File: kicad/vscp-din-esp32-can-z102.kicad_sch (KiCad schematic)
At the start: 33 parts, among them J1 Conn_01x05, J2 Conn_01x02, J3 Conn_01x06, J4 Conn_01x04, J5 Conn_01x04, J6 Conn_01x03, U1 ESP32-C3-WROOM-02-N4, U2 LM2575-3.3BT, U3 SN65HVD232, U4 R-78B3.3-1.0 (Recom)

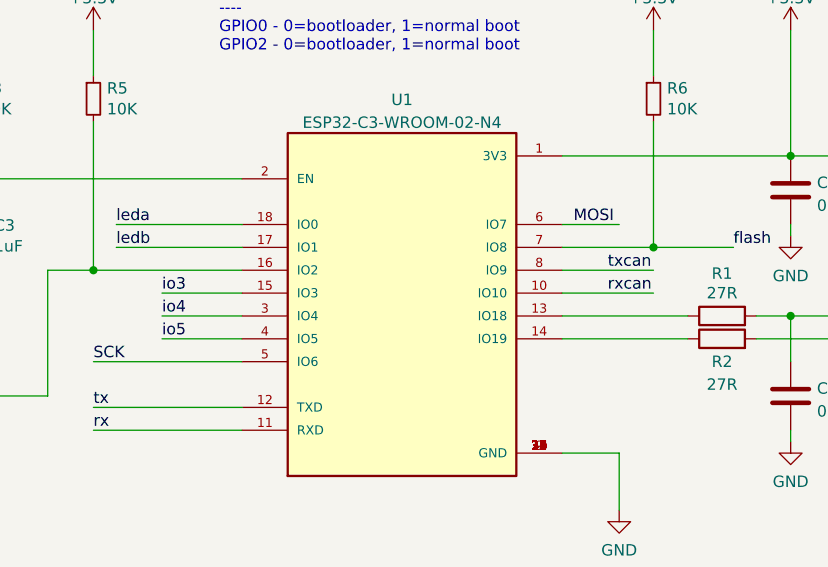
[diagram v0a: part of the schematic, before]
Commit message: rev b schame started canrx moved from gpio10 to gpio3
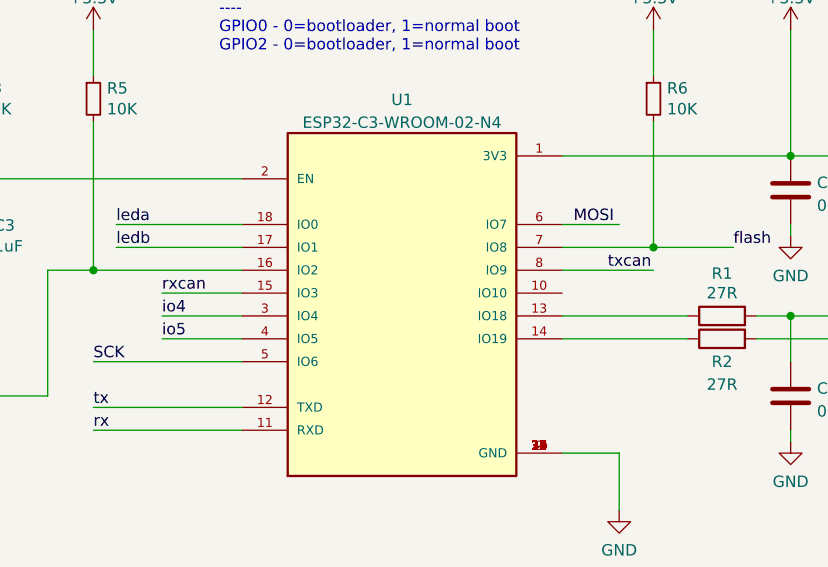
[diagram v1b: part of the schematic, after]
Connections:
- net io3 is gone; now on net rxcan: U1.15 (IO3)
- net rxcan: no longer U1.10 (IO10)
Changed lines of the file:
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@@
-    (stroke (width 0) (type default) (color 0 0 0 0))
-  )
-  (wire (pts (xy 134.62 57.15) (xy 144.78 57.15))
     (stroke (width 0) (type default) (color 0 0 0 0))
   )
@@
     (stroke (width 0) (type default) (color 0 0 0 0))
   )
+  (wire (pts (xy 68.58 46.99) (xy 68.58 44.45))
+    (stroke (width 0) (type default) (color 0 0 0 0))
+  )
+  (wire (pts (xy 262.89 148.59) (xy 262.89 153.67))
+    (stroke (width 0) (type default) (color 0 0 0 0))
+  )
+  (wire (pts (xy 82.55 107.95) (xy 97.79 107.95))
+    (stroke (width 0) (type default) (color 0 0 0 0))
+  )
+  (wire (pts (xy 148.59 121.92) (xy 160.02 121.92))
+    (stroke (width 0) (type default) (color 0 0 0 0))
+  )
+  (wire (pts (xy 208.28 81.28) (xy 215.9 81.28))
+    (stroke (width 0) (type default) (color 0 0 0 0))
+  )
+  (wire (pts (xy 240.03 93.98) (xy 240.03 97.79))
+    (stroke (width 0) (type default) (color 0 0 0 0))
+  )
+  (wire (pts (xy 138.43 158.75) (xy 138.43 160.02))
+    (stroke (width 0) (type default) (color 0 0 0 0))
+  )
+  (wire (pts (xy 144.78 52.07) (xy 153.67 52.07))
+    (stroke (width 0) (type default) (color 0 0 0 0))
+  )
+  (wire (pts (xy 160.02 129.54) (xy 160.02 156.21))
+    (stroke (width 0) (type default) (color 0 0 0 0))
+  )
+  (wire (pts (xy 90.17 62.23) (xy 99.06 62.23))
+    (stroke (width 0) (type default) (color 0 0 0 0))
+  )
+  (wire (pts (xy 99.06 54.61) (xy 82.55 54.61))
+    (stroke (width 0) (type default) (color 0 0 0 0))
+  )
+  (wire (pts (xy 134.62 52.07) (xy 144.78 52.07))
+    (stroke (width 0) (type default) (color 0 0 0 0))
+  )
+  (wire (pts (xy 226.06 35.56) (xy 226.06 26.67))
+    (stroke (width 0) (type default) (color 0 0 0 0))
+  )
   (wire (pts (xy 90.17 57.15) (xy 99.06 57.15))
-    (stroke (width 0) (type default) (color 0 0 0 0))
-  )
-  (wire (pts (xy 68.58 46.99) (xy 68.58 44.45))
-    (stroke (width 0) (type default) (color 0 0 0 0))
-  )
-  (wire (pts (xy 262.89 148.59) (xy 262.89 153.67))
-    (stroke (width 0) (type default) (color 0 0 0 0))
-  )
-  (wire (pts (xy 82.55 107.95) (xy 97.79 107.95))
-    (stroke (width 0) (type default) (color 0 0 0 0))
-  )
-  (wire (pts (xy 148.59 121.92) (xy 160.02 121.92))
-    (stroke (width 0) (type default) (color 0 0 0 0))
-  )
-  (wire (pts (xy 208.28 81.28) (xy 215.9 81.28))
-    (stroke (width 0) (type default) (color 0 0 0 0))
-  )
-  (wire (pts (xy 240.03 93.98) (xy 240.03 97.79))
-    (stroke (width 0) (type default) (color 0 0 0 0))
-  )
-  (wire (pts (xy 138.43 158.75) (xy 138.43 160.02))
-    (stroke (width 0) (type default) (color 0 0 0 0))
-  )
-  (wire (pts (xy 144.78 52.07) (xy 153.67 52.07))
-    (stroke (width 0) (type default) (color 0 0 0 0))
-  )
-  (wire (pts (xy 160.02 129.54) (xy 160.02 156.21))
-    (stroke (width 0) (type default) (color 0 0 0 0))
-  )
-  (wire (pts (xy 90.17 62.23) (xy 99.06 62.23))
-    (stroke (width 0) (type default) (color 0 0 0 0))
-  )
-  (wire (pts (xy 99.06 54.61) (xy 82.55 54.61))
-    (stroke (width 0) (type default) (color 0 0 0 0))
-  )
-  (wire (pts (xy 134.62 52.07) (xy 144.78 52.07))
-    (stroke (width 0) (type default) (color 0 0 0 0))
-  )
-  (wire (pts (xy 226.06 35.56) (xy 226.06 26.67))
     (stroke (width 0) (type default) (color 0 0 0 0))
   )
@@
     (effects (font (size 1.27 1.27)) (justify left bottom))
   )
-  (label "rxcan" (at 139.7 57.15 0)
+  (label "rxcan" (at 90.17 57.15 0)
     (effects (font (size 1.27 1.27)) (justify left bottom))
   )
@@
     (effects (font (size 1.27 1.27)) (justify left bottom))
   )
-  (label "io3" (at 90.17 57.15 0)
-    (effects (font (size 1.27 1.27)) (justify left bottom))
-  )

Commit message: Added images for rev B
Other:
- note removed: "A"
- company: (none) -> Grodans Paradis AB
- title: (none) -> vscp-din-esp32-can-z102
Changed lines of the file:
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@@
 (kicad_sch (version 20211123) (generator eeschema)
   (paper "A4")
+  (title_block
+    (title "vscp-din-esp32-can-z102")
+    (rev "B")
+    (company "Grodans Paradis AB")
+  )
   (junction (at 30.48 156.21) (diameter 0) (color 0 0 0 0)
   )
@@
     (stroke (width 0) (type default) (color 0 0 0 0))
   )
+  (wire (pts (xy 144.78 52.07) (xy 151.13 52.07))
+    (stroke (width 0) (type default) (color 0 0 0 0))
+  )
   (wire (pts (xy 160.02 121.92) (xy 189.23 121.92))
     (stroke (width 0) (type default) (color 0 0 0 0))
@@
   )
   (wire (pts (xy 138.43 158.75) (xy 138.43 160.02))
-    (stroke (width 0) (type default) (color 0 0 0 0))
-  )
-  (wire (pts (xy 144.78 52.07) (xy 153.67 52.07))
     (stroke (width 0) (type default) (color 0 0 0 0))
   )
@@
     (effects (font (size 1.27 1.27)) (justify left bottom))
   )
-  (text "A" (at 270.51 194.31 0)
-    (effects (font (size 1.27 1.27)) (justify left bottom))
-  )
   (text "Programming\nInterface" (at 264.16 95.25 0)
     (effects (font (size 1.27 1.27)) (justify left bottom))
@@
     (effects (font (size 1.27 1.27)) (justify left bottom))
   )
-  (label "flash" (at 153.67 52.07 0)
+  (label "flash" (at 146.05 52.07 0)
     (effects (font (size 1.27 1.27)) (justify left bottom))
   )
@@
   )
   (symbol (lib_id "Device:L_Ferrite") (at 87.63 161.29 90) (unit 1)
-    (in_bom yes) (on_board yes) (fields_autoplaced)
-    (property "Reference" "L1" (id 0) (at 87.63 156.1932 90))
+    (in_bom yes) (on_board yes)
+    (property "Reference" "L1" (id 0) (at 87.63 162.56 90))
     (property "Value" "SRR1240-331K" (id 1) (at 87.63 158.7301 90))
     (property "Footprint" "Inductor_SMD:L_Bourns_SRR1260" (id 2) (at 87.63 161.29 0)

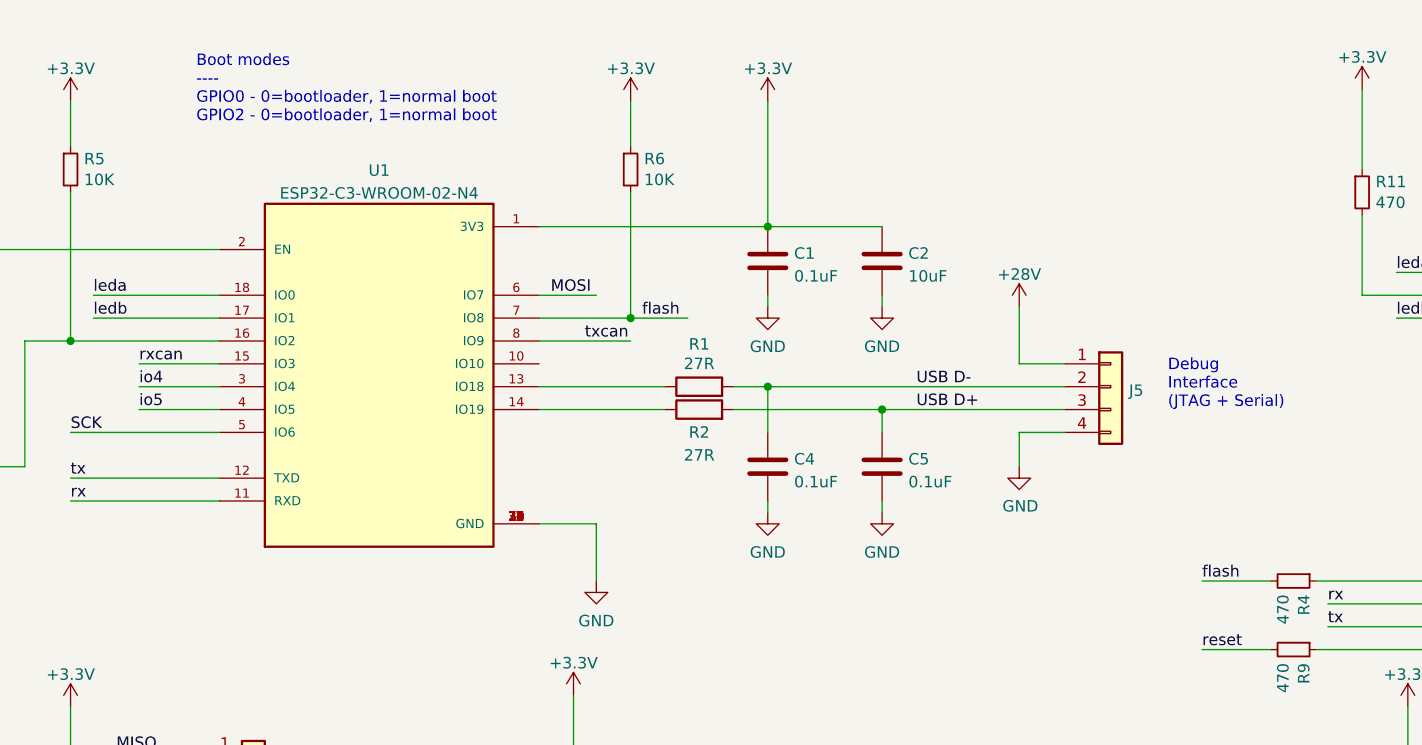
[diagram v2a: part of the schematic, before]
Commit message: txcan routed to Flash pin instead of io8
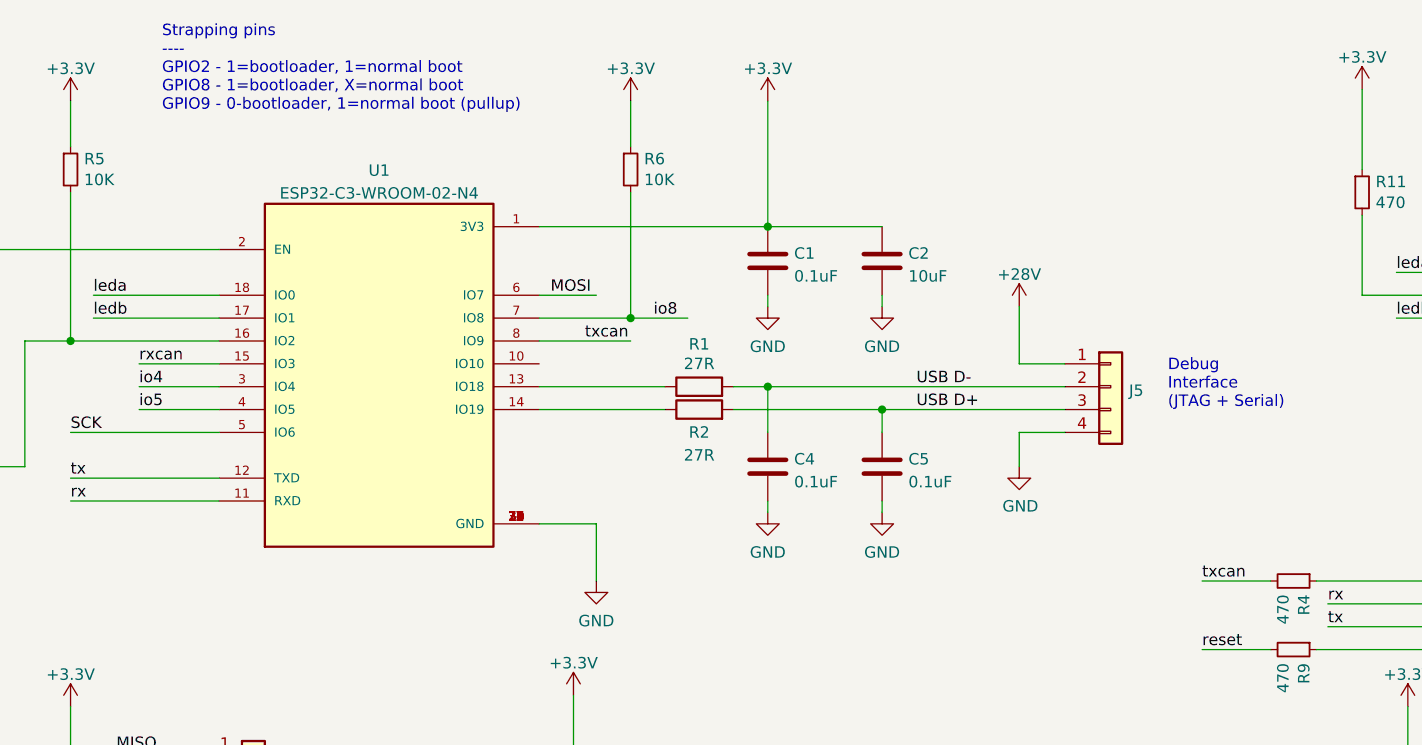
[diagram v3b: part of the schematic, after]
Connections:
- net txcan: now also R4.2
- net flash renamed io8
- net io8: no longer R4.2
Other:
- note added: "Strapping pins ---- GPIO2 - 1=bootloader, 1=normal boot GPIO8 - 1=bootloader, X=normal boot GPIO9 - 0-bootloader, 1=normal boot (pullup)"
- note removed: "Boot modes ---- GPIO0 - 0=bootloader, 1=normal boot GPIO2 - 0=bootloader, 1=normal boot"
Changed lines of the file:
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@@
     (effects (font (size 1.27 1.27)) (justify left bottom))
   )
-  (text "Boot modes\n----\nGPIO0 - 0=bootloader, 1=normal boot\nGPIO2 - 0=bootloader, 1=normal boot"
-    (at 96.52 30.48 0)
+  (text "Strapping pins\n----\nGPIO2 - 1=bootloader, 1=normal boot\nGPIO8 - 1=bootloader, X=normal boot\nGPIO9 - 0-bootloader, 1=normal boot (pullup)"
+    (at 92.71 29.21 0)
     (effects (font (size 1.27 1.27)) (justify left bottom))
   )
@@
     (effects (font (size 1.27 1.27)) (justify left bottom))
   )
-  (label "flash" (at 208.28 81.28 0)
-    (effects (font (size 1.27 1.27)) (justify left bottom))
-  )
   (label "reset" (at 208.28 88.9 0)
     (effects (font (size 1.27 1.27)) (justify left bottom))
@@
   )
   (label "rxcan" (at 90.17 57.15 0)
+    (effects (font (size 1.27 1.27)) (justify left bottom))
+  )
+  (label "io8" (at 147.32 52.07 0)
+    (effects (font (size 1.27 1.27)) (justify left bottom))
+  )
+  (label "txcan" (at 208.28 81.28 0)
     (effects (font (size 1.27 1.27)) (justify left bottom))
   )
@@
     (effects (font (size 1.27 1.27)) (justify left bottom))
   )
-  (label "flash" (at 146.05 52.07 0)
-    (effects (font (size 1.27 1.27)) (justify left bottom))
-  )

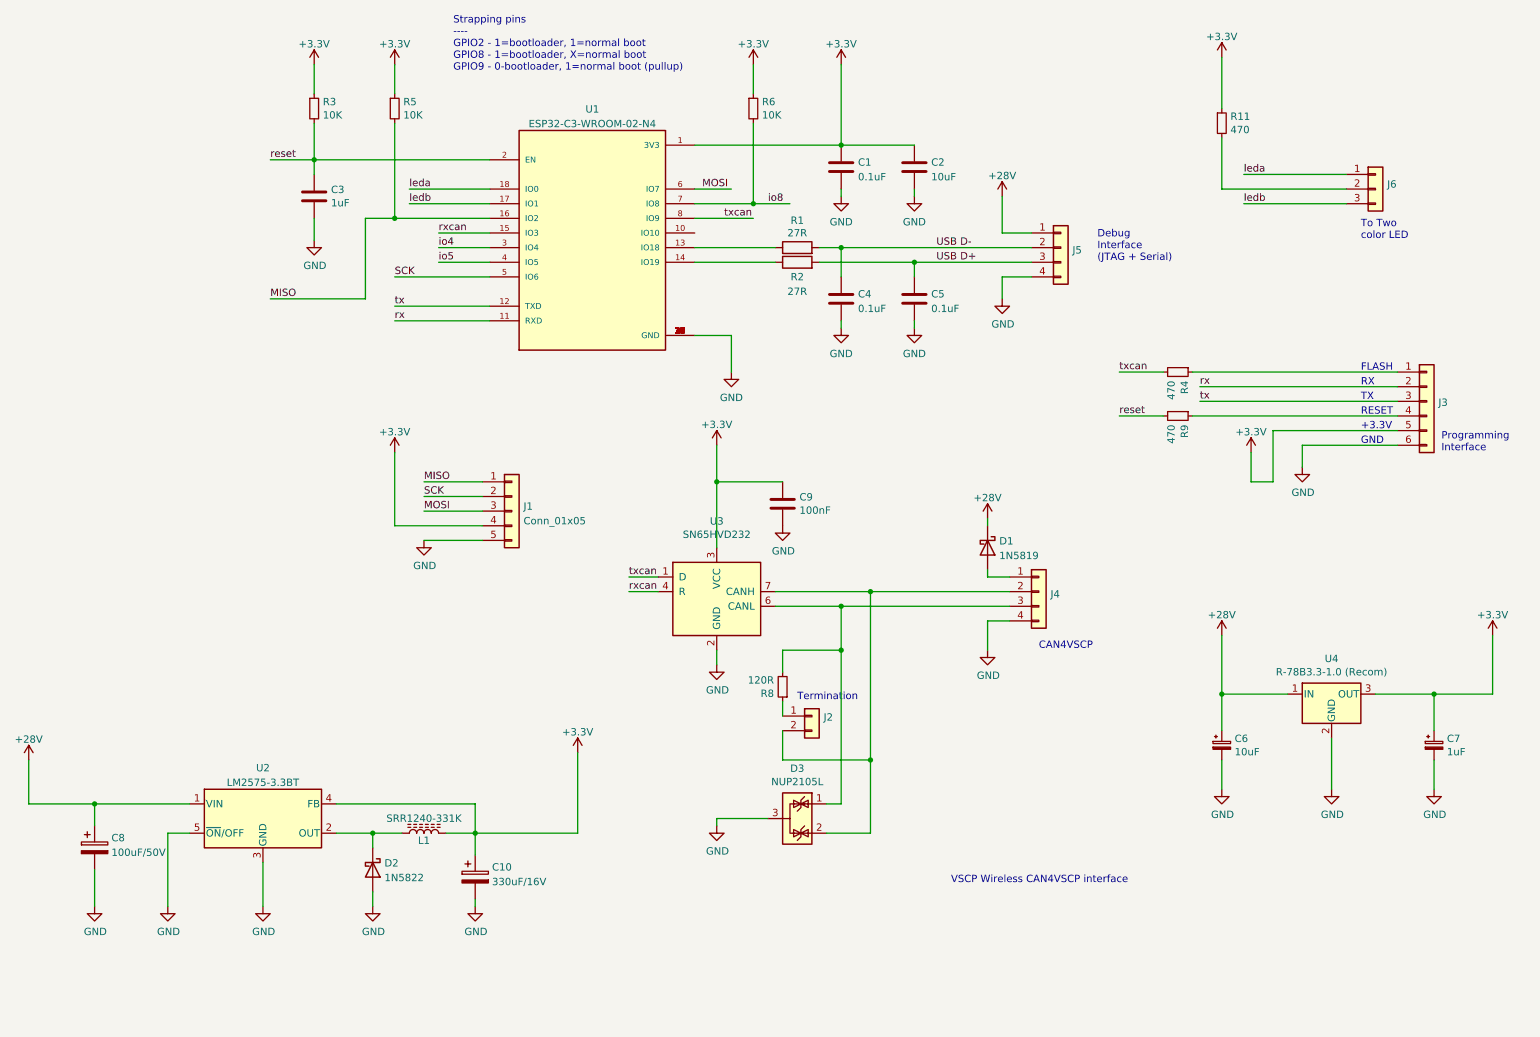
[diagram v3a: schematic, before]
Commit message: Added connector and resistor for BUS_OFF LED connector.
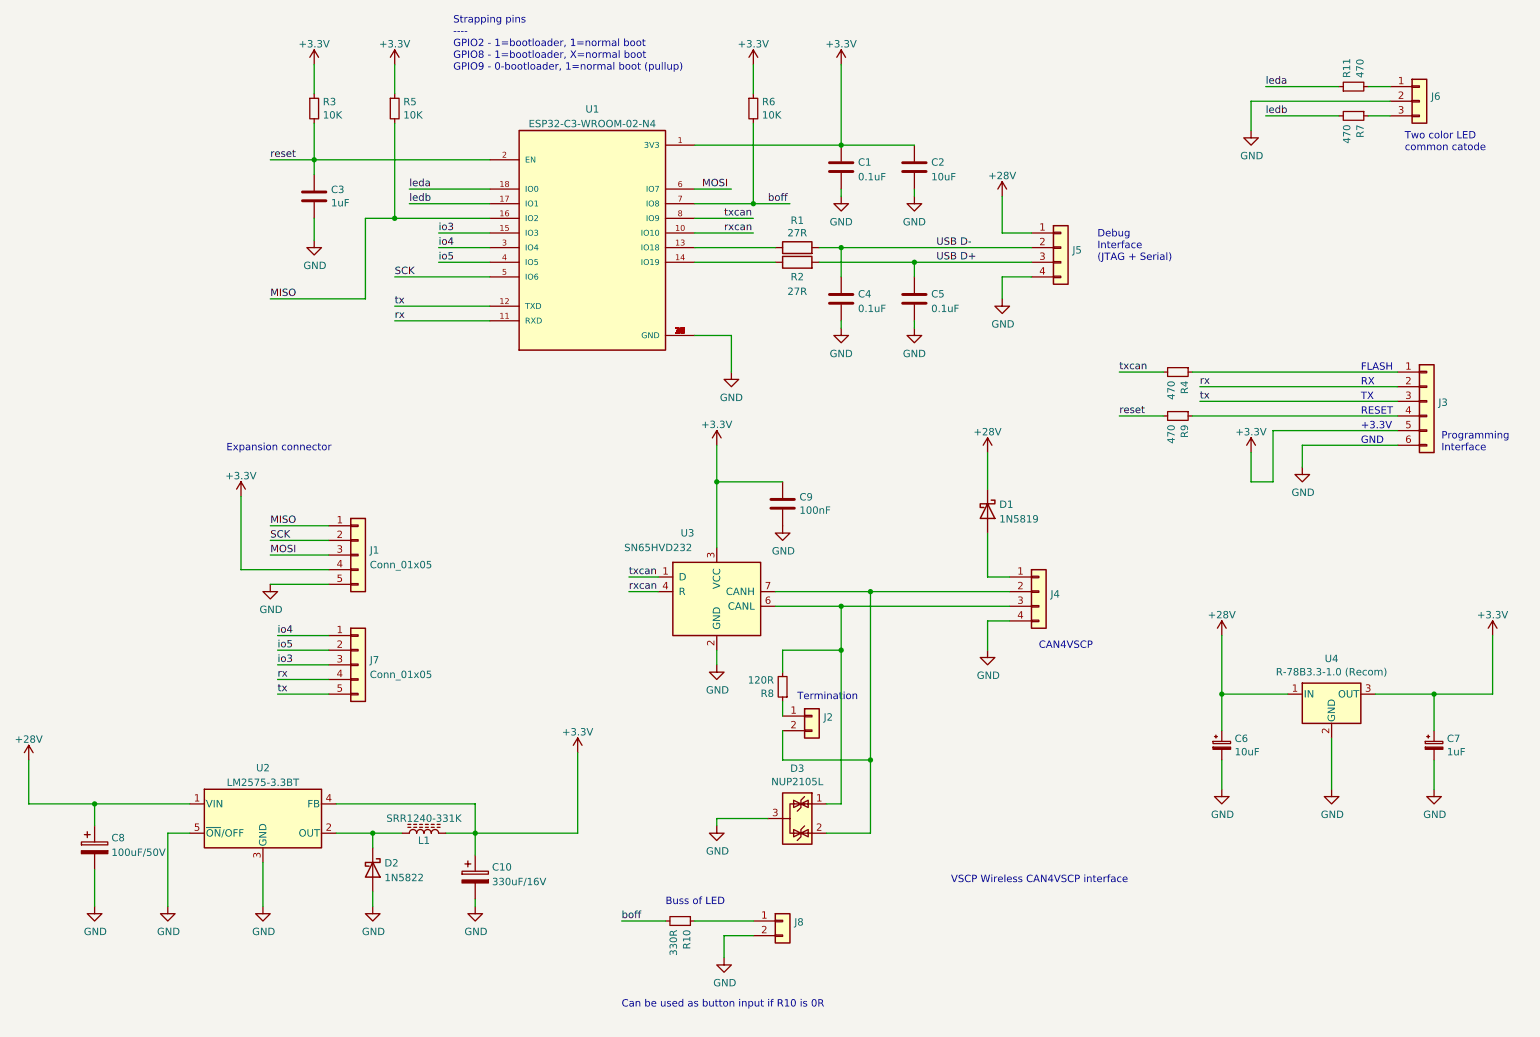
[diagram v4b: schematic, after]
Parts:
- added J7: Conn_01x05, Connector_PinHeader_2.54mm:PinHeader_1x05_P2.54mm_Vertical, symbol Connector_Generic:Conn_01x05
- added J8: Conn_01x02, Connector_PinHeader_2.54mm:PinHeader_1x02_P2.54mm_Vertical, symbol Connector_Generic:Conn_01x02
- added R10: 330R, Resistor_SMD:R_0805_2012Metric_Pad1.20x1.40mm_HandSolder, symbol Device:R_Small
- added R7: 470, Resistor_SMD:R_0805_2012Metric, symbol Device:R_Small
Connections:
- net +3V3: no longer R11.1
- net GND: now also J6.2 (Pin_2), J8.2 (Pin_2)
- net io4: now also J7.1 (Pin_1)
- net io5: now also J7.2 (Pin_2)
- net leda: now also R11.1; no longer J6.1 (Pin_1)
- net ledb: now also R7.2; no longer J6.3 (Pin_3)
- net rx: now also J7.4 (Pin_4)
- net rxcan: now also U1.10 (IO10); no longer U1.15 (IO3)
- net tx: now also J7.5 (Pin_5)
- net at R11.2: now also J6.1 (Pin_1); no longer J6.2 (Pin_2)
- net io8 renamed boff
- net boff: now also R10.2
- new net: J8.1 (Pin_1), R10.1
- new net: J6.3 (Pin_3), R7.1
- new net io3: J7.3 (Pin_3), U1.15 (IO3)
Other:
- note added: "Buss of LED"
- note added: "Can be used as button input if R10 is 0R"
- note added: "Expansion connector"
- note added: "Two color LED common catode"
- note removed: "To Two color LED"
- moved on the sheet: D1, J1, J6, R11
